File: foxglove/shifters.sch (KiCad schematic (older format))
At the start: 38 parts

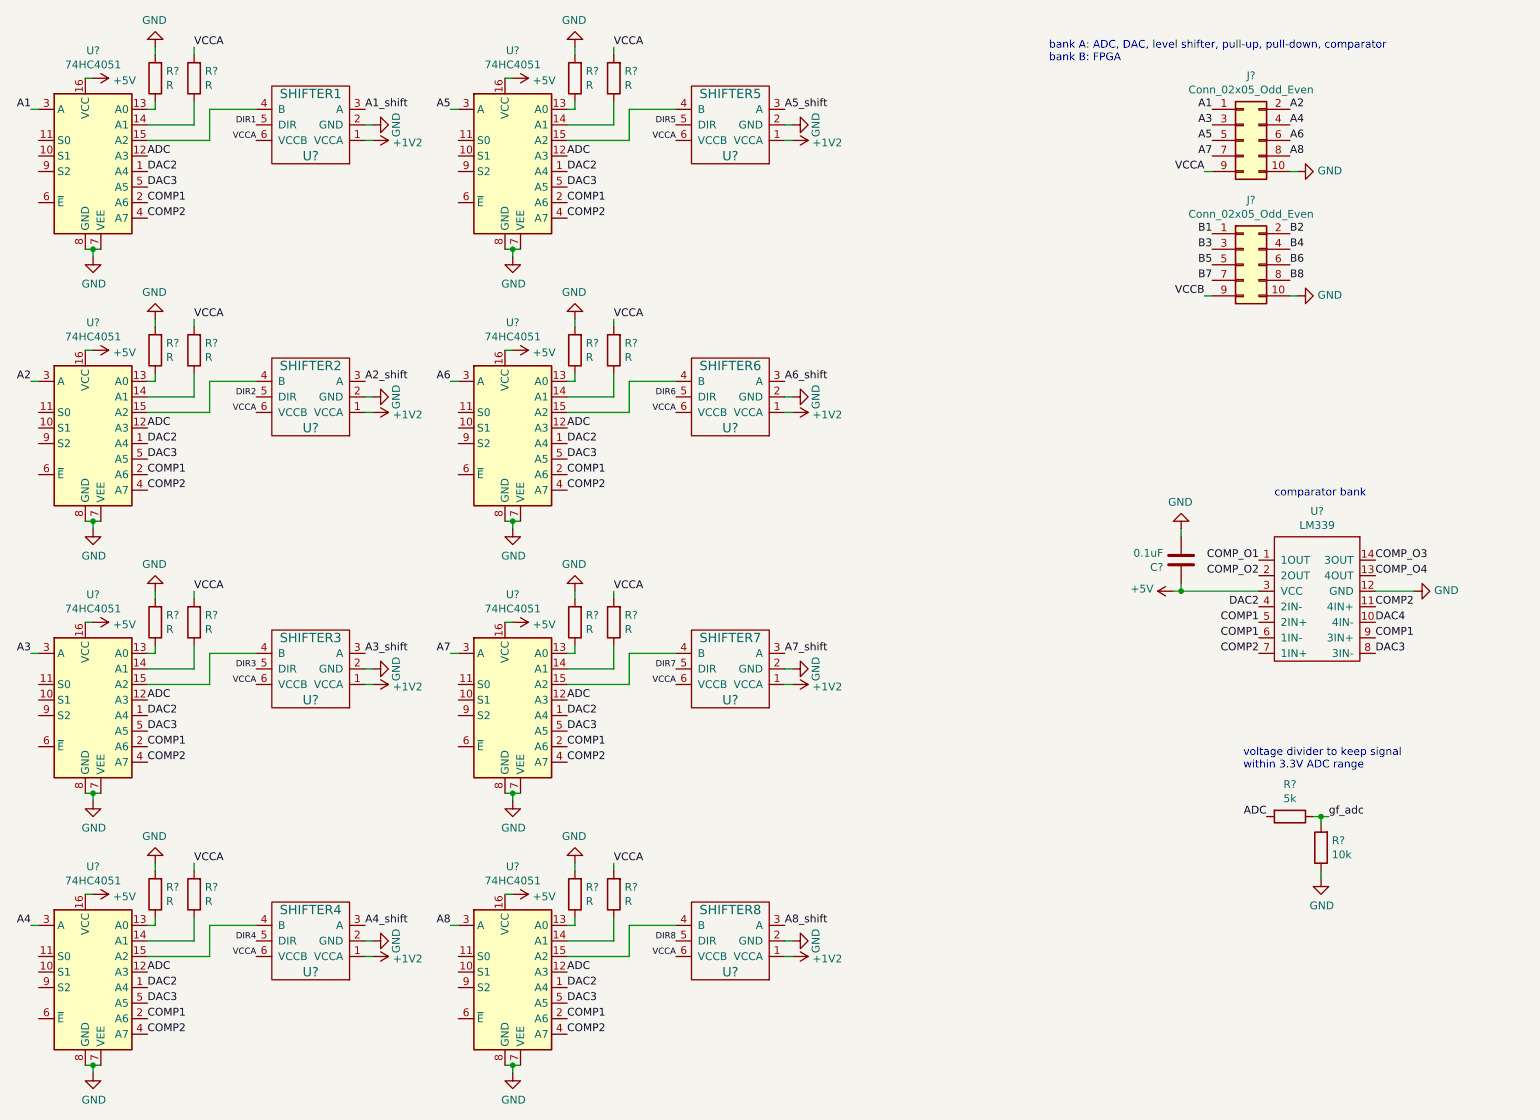
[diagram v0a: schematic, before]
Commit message: Added iCE40-HX8K-CT256 to schematic, began signal routing.
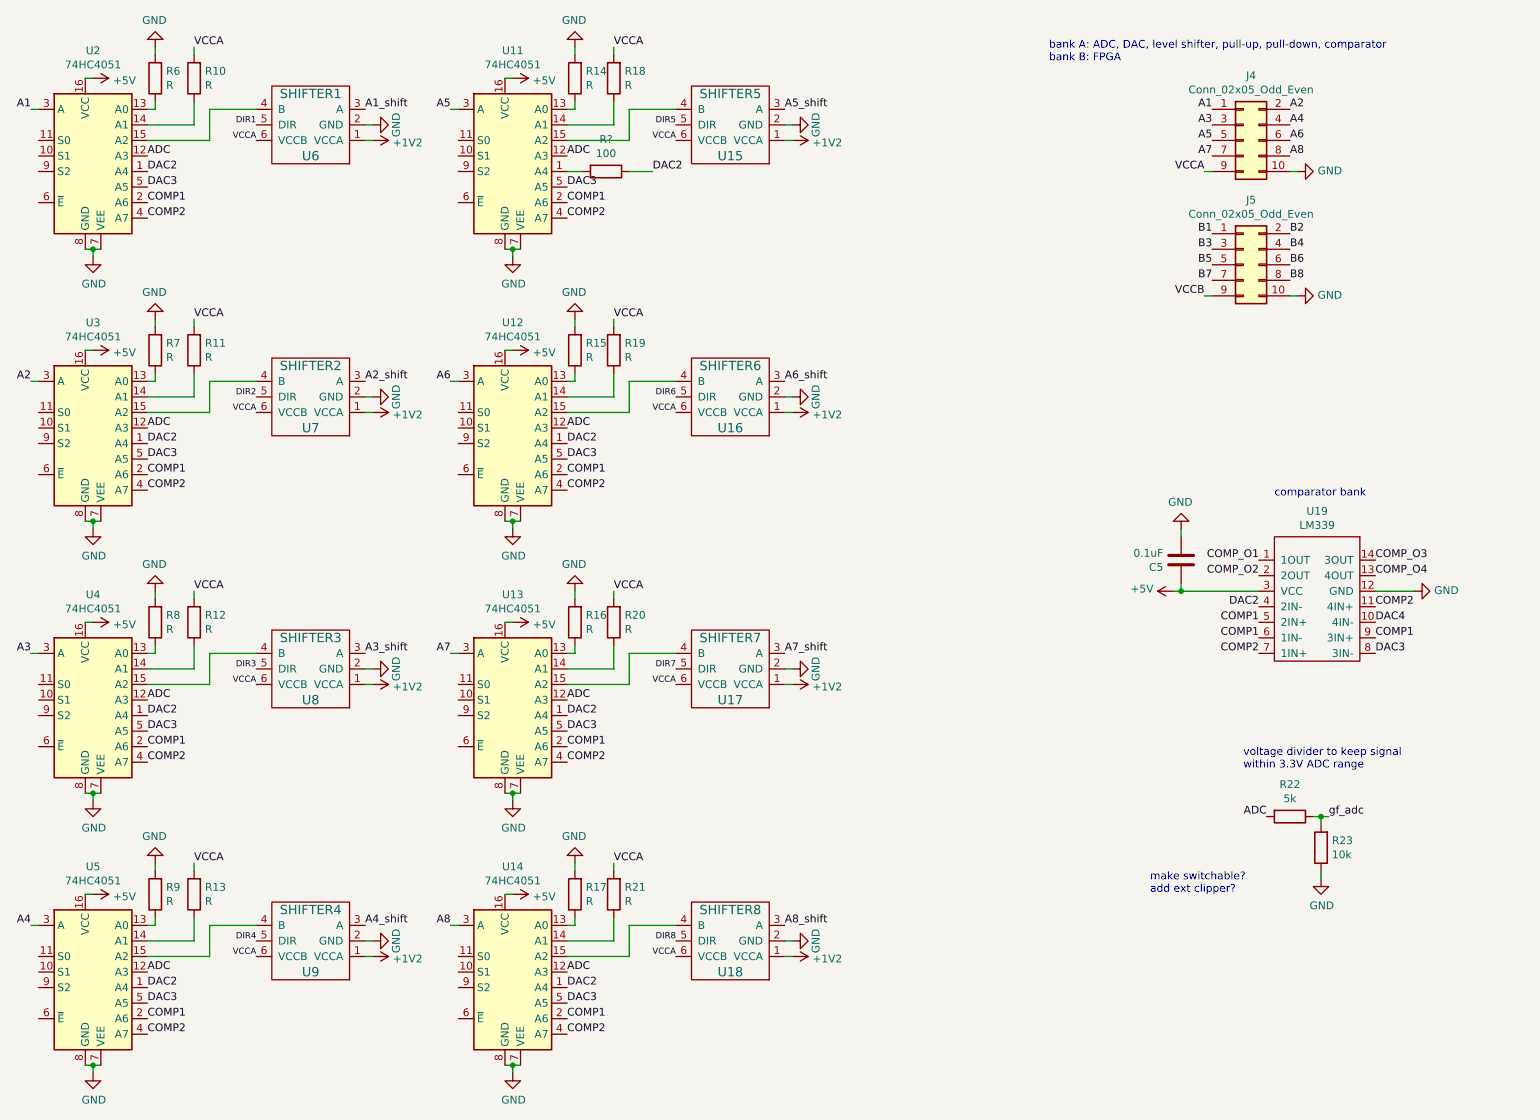
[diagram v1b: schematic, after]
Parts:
- added R?: 100, symbol Device:R
- gave numbers to parts that had none: 38
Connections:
- net DAC2: now also R?.1; no longer U11.1 (A4)
- new net: R?.2, U11.1 (A4)
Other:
- note added: "make switchable?\nadd ext clipper?"
